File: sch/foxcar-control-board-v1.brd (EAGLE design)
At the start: 160 x 100 mm, 114 parts, among them J1 USB_MICROB, J2 MICROSD, J3 XBEE-PRO, U1 SPX29300, U2 HMC5883LSMD, U3 STM32F4V, U4 VNH5019, U6 MPU6000

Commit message: Making much better progress on stm32. relocating to house because I live in a land of less-than-24-hour coffee shops. :(
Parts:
- TP2: value TPTP06R -> (none)
- moved JP38 29.7 mm to (74.0, 33.3)
- moved JP37 28.2 mm to (76.8, 33.7)
- moved JP2 27.6 mm to (93.0, 33.3), turned to 180 degrees
- moved JP36 26.0 mm to (79.7, 33.3)
- moved JP35 23.5 mm to (82.5, 33.7)
- moved JP6 20.4 mm to (103.8, 33.3)
- moved C4 8.96 mm to (73.7, 42.2), turned to 270 degrees
- moved CTS1 6.33 mm to (77.8, 41.3)
- moved R14 5.72 mm to (35.2, 69.5)
- moved C5 4.24 mm to (81.9, 40.0), turned to 90 degrees
- moved C8 2.42 mm to (76.8, 45.4), turned to 0 degrees
- moved TP2 2.25 mm to (81.9, 45.1)
- moved C20 1.59 mm to (85.4, 43.2)
- moved R8 1.42 mm to (81.9, 43.2)
- moved C11 1.35 mm to (72.7, 65.4), turned to 270 degrees
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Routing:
- net N$16: track 0.00 -> 22.5 mm, vias 0 -> 1
- net N$10: track 0.00 -> 22.3 mm, vias 0 -> 1
- net N$9: track 0.00 -> 21.8 mm, vias 0 -> 1
- net N$14: track 0.00 -> 21.5 mm, vias 0 -> 1
- net TX2: track 0.00 -> 19.0 mm
- net RX1: track 0.00 -> 15.3 mm
- net TX1: track 0.00 -> 14.7 mm
- net OSC_IN1: track 0.00 -> 13.1 mm
- net OSC_OUT1: track 0.00 -> 12.5 mm
- net 3.3V: track 14.2 -> 25.8 mm
- net GND: track 7.37 -> 16.1 mm, vias 5 -> 13
- net NRST: track 0.00 -> 4.87 mm

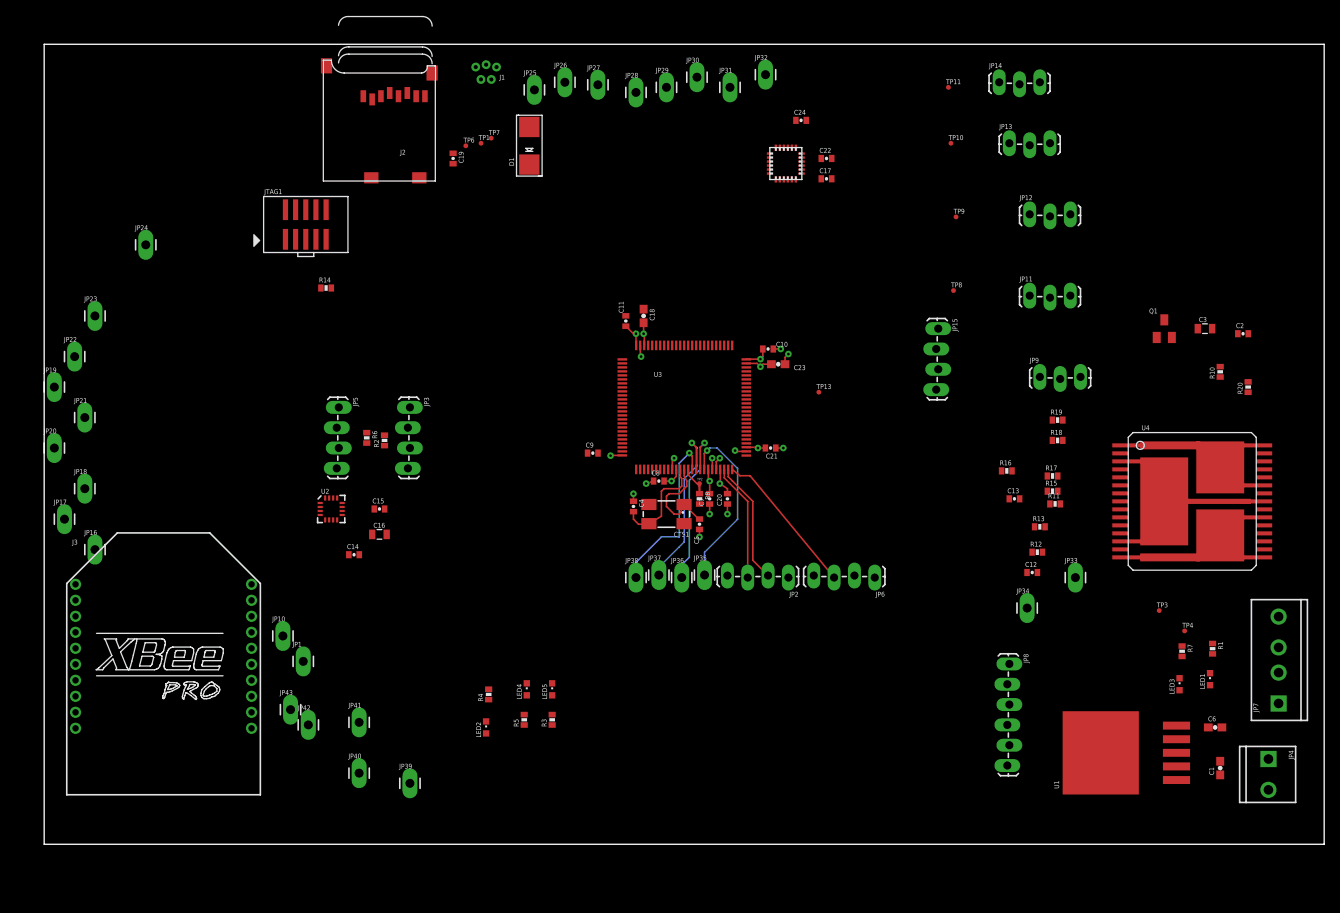
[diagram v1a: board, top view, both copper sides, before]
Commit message: Everything laid out except for the power stuff.
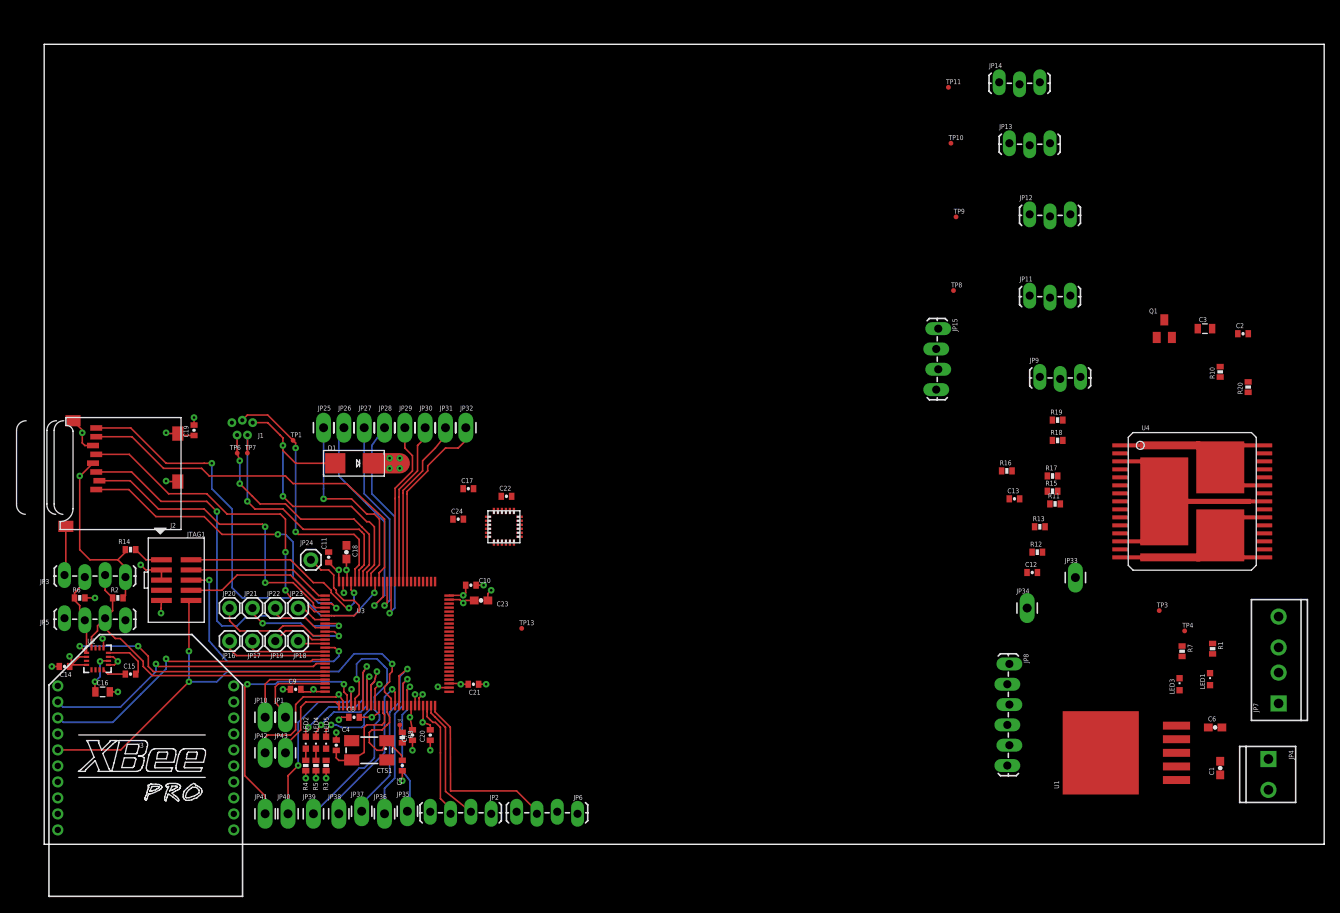
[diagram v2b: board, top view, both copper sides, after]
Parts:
- J1: value USB_MICROB -> (none)
- JP16, JP17, JP18, JP19, JP20, JP21, JP22, JP23, JP24: device SparkFun-Connectors:1X01_LONGPAD -> SparkFun-Connectors:1X01
- TP1, TP6, TP7: value TPTP06R -> (none)
- moved C24 65.7 mm to (51.8, 40.6)
- moved C17 59.2 mm to (53.0, 44.5)
- moved C22 58.2 mm to (57.8, 43.5)
- moved JP32 57.9 mm to (52.7, 52.1)
- moved U6 57.5 mm to (57.5, 39.7), turned to 90 degrees
- moved JP31 55.4 mm to (50.2, 52.1)
- moved JP30 55.4 mm to (47.6, 52.1)
- moved J1 53.9 mm to (24.8, 51.8)
- moved JP29 53.7 mm to (45.1, 52.1)
- moved JP28 52.4 mm to (42.5, 52.1)
- moved JP27 51.9 mm to (40.0, 52.1)
- moved JP26 51.3 mm to (37.5, 52.1)
- moved TP7 49.8 mm to (25.4, 48.9)
- moved JP25 49.8 mm to (34.9, 52.1)
- moved C8 48.2 mm to (38.7, 15.9)
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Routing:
- net NRST: track 4.87 -> 64.7 mm, vias 0 -> 3
- net SDIO_D1: track 0.00 -> 54.8 mm, vias 0 -> 2
- net SDIO_CMD: track 0.00 -> 49.2 mm, vias 0 -> 2
- net SDIO_D0: track 0.00 -> 48.3 mm
- net SCL1: track 0.00 -> 44.6 mm, vias 0 -> 2
- net SDIO_CLK: track 0.00 -> 42.3 mm, vias 0 -> 2
- net SDA1: track 0.00 -> 42.2 mm
- net SDIO_D2: track 0.00 -> 40.4 mm, vias 0 -> 2
- net FS_VBUS: track 0.00 -> 39.9 mm, vias 0 -> 2
- net SDIO_D3: track 0.00 -> 39.1 mm, vias 0 -> 2
- net 3.3V: track 25.8 -> 64.7 mm, vias 9 -> 17
- net TX_DIN1: track 0.00 -> 37.9 mm, vias 0 -> 1
- net RX_DOUT1: track 0.00 -> 36.8 mm, vias 0 -> 1
- net FS_DP: track 0.00 -> 33.3 mm, vias 0 -> 2
- net FS_DM: track 0.00 -> 33.0 mm, vias 0 -> 1
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
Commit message: Layout done, screenshots uploaded, parts list added.
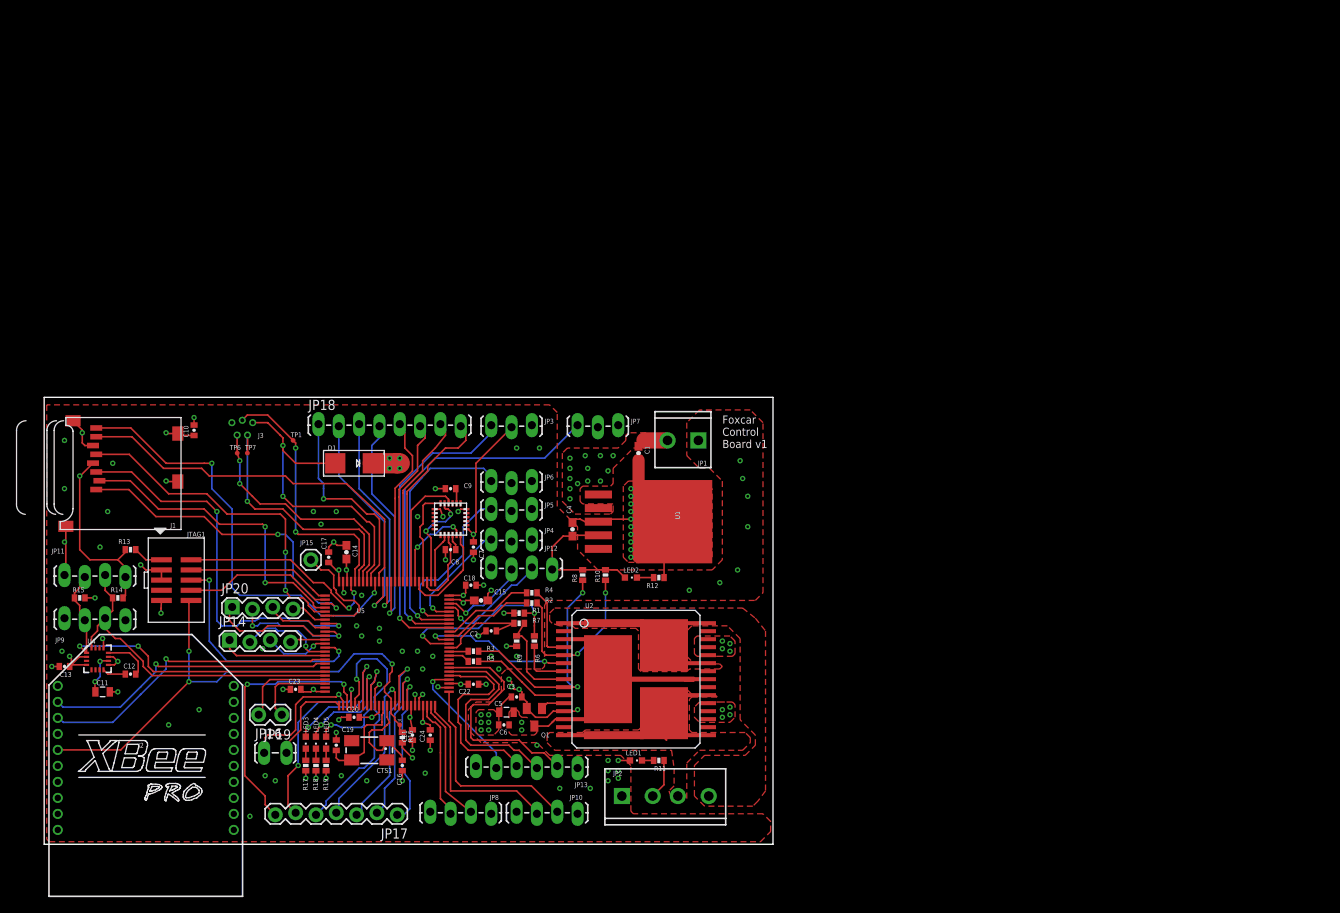
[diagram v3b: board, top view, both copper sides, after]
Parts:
- removed JP21, JP22, JP23, JP24: (no value), SparkFun-Connectors:1X01
- removed JP25, JP26, JP27, JP28, JP29, JP30, JP31, JP32, JP33, JP34, JP35, JP36, JP37, JP38, JP39, JP40, JP41, JP42, JP43: (no value), SparkFun-Connectors:1X01_LONGPAD
- removed R20: 4.7k, SparkFun-Passives:0402-RES
- removed TP10, TP11, TP13, TP3, TP4, TP8, TP9: TPTP06R, testpad:TP06R
- removed U6: MPU6000, invensense:QFN.24.4X4
- added R9: 1k, SparkFun-Passives:0402-RES
- added U5: STM32F4V, stm32f4:LQFP100
- C10: value 100nF -> 2.2uF
- C11: value 100nF -> 4.7uF; device SparkFun-Passives:0402-CAP -> SparkFun-Passives:0805
- C12: value 0.1uF -> 0.22uF
- C13: value 33nF -> 0.22uF
- C14, C15: value 0.22uF -> 2.2uF; device SparkFun-Passives:0402-CAP -> SparkFun-Passives:0603-CAP
- C16: value 4.7uF -> 16pF; device SparkFun-Passives:0805 -> SparkFun-Passives:0402-CAP
- C17, C22: value 0.1uF -> 100nF
- C18, C23: value 2.2uF -> 100nF; device SparkFun-Passives:0603-CAP -> SparkFun-Passives:0402-CAP
- C19: value 2.2uF -> 16pF
- C2: value 0.1uF -> 33nF
- C24: value 10nF -> 100nF
- C3: value 47uF -> 0.1uF; device SparkFun-Passives:0805 -> SparkFun-Passives:0402-CAP
- C4: value 16pF -> 10u; device SparkFun-Passives:0402-CAP -> SparkFun-Passives:0603-CAP
- C5: value 16pF -> 47uF; device SparkFun-Passives:0402-CAP -> SparkFun-Passives:0805
- C6: value 10u -> 0.1uF; device SparkFun-Passives:0603-CAP -> SparkFun-Passives:0402-CAP
- C7, C8: value 100nF -> 0.1uF
- C9: value 100nF -> 10nF
- J1: value (none) -> MICROSD; device SparkFun:MICRO-B-RA-TH -> adafruit:MICROSD
- J2: value MICROSD -> XBEE-PRO; device adafruit:MICROSD -> maxstream:XBEE-PRO
- J3: value XBEE-PRO -> (none); device maxstream:XBEE-PRO -> SparkFun:MICRO-B-RA-TH
- JP1: value (none) -> BATT; device SparkFun-Connectors:1X01_LONGPAD -> SparkFun-Connectors:SCREWTERMINAL-3.5MM-2_LOCK
- JP10: value (none) -> UART2; device SparkFun-Connectors:1X01_LONGPAD -> SparkFun-Connectors:1X04_LOCK_LONGPADS
- JP11: value ESCD -> I2C1-B; device SparkFun-Connectors:1X03_LOCK_LONGPADS -> SparkFun-Connectors:1X04_LOCK_LONGPADS
- JP12: value ESCC -> USART3; device SparkFun-Connectors:1X03_LOCK_LONGPADS -> SparkFun-Connectors:1X04_LOCK_LONGPADS
- JP13: value ESCB -> SPI1; device SparkFun-Connectors:1X03_LOCK_LONGPADS -> SparkFun-Connectors:1X06_LOCK_LONGPADS
- JP14: value ESCA -> (none); device SparkFun-Connectors:1X03_LOCK_LONGPADS -> SparkFun-Connectors:1X04_LOCK
- JP15: value USART3 -> (none); device SparkFun-Connectors:1X04_LOCK_LONGPADS -> SparkFun-Connectors:1X01
- JP16: device SparkFun-Connectors:1X01 -> SparkFun-Connectors:1X02_LOCK_LONGPADS
- JP17: device SparkFun-Connectors:1X01 -> SparkFun-Connectors:1X07_LOCK
- JP18: device SparkFun-Connectors:1X01 -> SparkFun-Connectors:1X08_LOCK_LONGPADS
- JP19: device SparkFun-Connectors:1X01 -> SparkFun-Connectors:1X02_LOCK
- JP2: value USART1 -> MOTORS; device SparkFun-Connectors:1X04_LOCK_LONGPADS -> SparkFun-Connectors:SCREWTERMINAL-3.5MM-4_LOCK
- JP20: device SparkFun-Connectors:1X01 -> SparkFun-Connectors:1X04_LOCK
- JP3: value I2C1-B -> SERVO; device SparkFun-Connectors:1X04_LOCK_LONGPADS -> SparkFun-Connectors:1X03_LOCK_LONGPADS
- JP4: value BATT -> ESCA; device SparkFun-Connectors:SCREWTERMINAL-3.5MM-2_LOCK -> SparkFun-Connectors:1X03_LOCK_LONGPADS
- JP5: value I2C1-A -> ESCB; device SparkFun-Connectors:1X04_LOCK_LONGPADS -> SparkFun-Connectors:1X03_LOCK_LONGPADS
- JP6: value UART2 -> ESCC; device SparkFun-Connectors:1X04_LOCK_LONGPADS -> SparkFun-Connectors:1X03_LOCK_LONGPADS
- JP7: value MOTORS -> ESCD; device SparkFun-Connectors:SCREWTERMINAL-3.5MM-4_LOCK -> SparkFun-Connectors:1X03_LOCK_LONGPADS
- JP8: value SPI1 -> USART1; device SparkFun-Connectors:1X06_LOCK_LONGPADS -> SparkFun-Connectors:1X04_LOCK_LONGPADS
- JP9: value SERVO -> I2C1-A; device SparkFun-Connectors:1X03_LOCK_LONGPADS -> SparkFun-Connectors:1X04_LOCK_LONGPADS
- LED2: value (none) -> GREEN
- LED3: value GREEN -> (none)
- R1: value 270 -> 10k
- R11: value 1k -> 270
- R12, R17, R18, R19: value 1k -> 50
- R13: value 1k -> 100
- R14: value 100 -> 1.5k
- R15: value 10k -> 1.5k
- R2, R6: value 1.5k -> 1k
- R3, R4, R5: value 50 -> 1k
- R7: value 50 -> 10k
- R8: value 10k -> 4.7k
- U2: value HMC5883LSMD -> VNH5019; device SparkFun-Sensors:16LPCC -> wicker:MULTIPOWERSO-30
- U3: value STM32F4V -> MPU6000; device stm32f4:LQFP100 -> invensense:QFN.24.4X4
- U4: value VNH5019 -> HMC5883LSMD; device wicker:MULTIPOWERSO-30 -> SparkFun-Sensors:16LPCC
- moved U4 138.3 mm to (6.67, 23.2), turned to 0 degrees
- moved JP11 125.6 mm to (2.54, 33.7)
- moved JP9 125.6 mm to (2.54, 28.3)
- moved R15 122.3 mm to (4.45, 30.8)
- moved C13 120.6 mm to (2.54, 22.2), turned to 180 degrees
- moved JP14 118.9 mm to (23.2, 25.4)
- moved R13 113.7 mm to (10.8, 36.8), turned to 180 degrees
- moved C12 113.4 mm to (10.8, 21.3)
- moved LED3 109.5 mm to (32.7, 12.7), turned to 180 degrees
- moved R18 101.2 mm to (34.0, 9.84), turned to 90 degrees
- moved R19 101.1 mm to (35.2, 9.84), turned to 90 degrees
- moved C2 101.1 mm to (55.9, 26.7), turned to 180 degrees
- moved JP4 101.0 mm to (55.9, 38.1), turned to 0 degrees
- moved R17 100.1 mm to (32.7, 9.84), turned to 90 degrees
- moved C3 97.6 mm to (59.1, 18.4), turned to 180 degrees
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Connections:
- removed net N$13: C17.1, U6.10
- removed net N$17: JP34.1, U3.PC4
- removed net N$8: JP33.1, U3.PC5
- new net REGOUT: C8.1, U3.10
- net 3.3V: now also C13.1, C14.2, C15.2, C17.2, C22.2, C24.2, C4.1, C7.1, J1.4, J2.1, J2.14, JP10.4, JP11.4, JP12.4, JP13.6, JP3.2, JP8.4, JP9.4, LED2.A, R13.2, R15.2, R16.2, R17.1, R18.1, R19.1, U3.13, U4.13, U4.2, U4.4, U5.VCAP1, U5.VCAP2, U5.VDD1, U5.VDD2, U5.VDD3, U5.VDD4, U5.VDD5, U5.VDD6, U5.VDDA; no longer C11.2, C14.1, C19.2, C22.1, C6.1, C7.2, C8.2, C9.2, J2.4, J3.1, J3.14, JP15.4, JP2.4, JP3.4, JP5.4, JP6.4, JP8.6, JP9.2, LED3.A, R2.2, R20.2, R3.1, R4.1, R5.1, R6.2, TP4.TP, U2.13, U2.2, U2.4, U3.VCAP1, U3.VCAP2, U3.VDD1, U3.VDD2, U3.VDD3, U3.VDD4, U3.VDD5, U3.VDD6, U3.VDDA, U6.13
- net CP: now also U2.11; no longer U4.11
- net CS: now also R7.2, R9.2, U2.8; no longer R11.2, R15.2, U4.8
- net DIR: now also JP3.1, U5.PE11; no longer JP9.1, TP13.TP, U3.PE11
- net ENA: now also R10.1, R2.2, U2.5; no longer R18.2, R20.1, U4.5
- net ENB: now also R3.2, R8.1, U2.9; no longer R10.1, R13.2, U4.9
- net ESCA: now also JP4.1, U5.PE15; no longer JP14.1, TP11.TP, U3.PE15
- net ESCB: now also JP5.1, U5.PE14; no longer JP13.1, TP10.TP, U3.PE14
- net ESCC: now also JP6.1, U5.PE13; no longer JP12.1, TP9.TP, U3.PE13
- net ESCD: now also JP7.1, U5.PE12; no longer JP11.1, TP8.TP, U3.PE12
- net FS_DM: now also J3.2, U5.PA11; no longer J1.2, U3.PA11
- net FS_DP: now also J3.3, U5.PA12; no longer J1.3, U3.PA12
- net FS_ID: now also J3.4, U5.PA10; no longer J1.4, U3.PA10
- net FS_VBUS: now also J3.1, U5.PA9; no longer J1.1, U3.PA9
- net GND: now also C11.2, C14.1, C15.1, C16.1, C17.1, C22.1, C24.1, C4.2, C5.2, C7.2, C8.2, C9.2, J1.6, J1.CD1, J1.CD2, J1.MT1, J1.MT2, J2.10, J3.5, JP1.1, JP10.1, JP11.1, JP12.1, JP13.1, JP2.2, JP3.3, JP9.1, R12.1, R9.1, U2.18, U2.19, U2.20, U2.26, U2.27, U2.28, U3.1, U3.18, U4.11, U4.9, U5.VREF+, U5.VSS1, U5.VSS2, U5.VSS3, U5.VSSA; no longer C11.1, C12.2, C14.2, C16.2, C17.2, C22.2, C24.2, C4.1, C5.1, C7.1, C8.1, C9.1, J1.5, J2.6, J2.CD1, J2.CD2, J2.MT1, J2.MT2, J3.10, JP15.1, JP2.1, JP3.1, JP4.1, JP5.1, JP6.1, JP7.2, JP9.3, R16.1, R7.1, U2.11, U2.9, U3.VREF+, U3.VSS1, U3.VSS2, U3.VSS3, U3.VSSA, U4.18, U4.19, U4.20, U4.26, U4.27, U4.28, U6.1, U6.18
- net IMU_CLKOUT: now also U3.22, U5.PD10; no longer U3.PD10, U6.22
- net IMU_FSYNC: now also U3.11, U5.PD9; no longer U3.PD9, U6.11
- net IMU_INT: now also U3.12, U5.PD8; no longer U3.PD8, U6.12
- net INA: now also R4.2, U2.4; no longer R19.2, U4.4
- net INB: now also R5.2, U2.10; no longer R12.2, U4.10
- net LED_B: now also U5.PC15; no longer U3.PC15
- net LED_G: now also U5.PC14; no longer U3.PC14
- net LED_R: now also LED3.A, U5.PC13; no longer LED2.A, U3.PC13
- net MD_CS: now also C2.1, R7.1, U5.PB2; no longer C13.1, R15.1, U3.PB2
- net MD_CSDIS: now also U2.6, U5.PE8; no longer U3.PE8, U4.6
- net MD_ENA: now also R2.1, U5.PE9; no longer R18.1, U3.PE9
- net MD_ENB: now also R3.1, U5.PB1; no longer R13.1, U3.PB1
- net MD_INA: now also R4.1, U5.PE10; no longer R19.1, U3.PE10
- net MD_INB: now also R5.1, U5.PB0; no longer R12.1, U3.PB0
- net MD_PWM: now also R1.2, R6.1, U5.PE7; no longer R16.2, R17.1, U3.PE7
- net N$1: now also JP18.1, U5.PA8; no longer JP25.1, U3.PA8
- net N$10: now also JP17.3, U5.PC1; no longer JP37.1, U3.PC1
- net N$11: now also C12.1, U4.8; no longer C15.1, U2.8
- net N$12: now also C11.1, U4.10; no longer C16.1, U2.10
- net N$14: now also JP17.2, U5.PC2; no longer JP36.1, U3.PC2
- net N$15: now also JP19.1, U5.PE1; no longer JP1.1, U3.PE1
- net N$16: now also JP17.1, U5.PC3; no longer JP35.1, U3.PC3
- net N$18: now also C9.1, U3.20; no longer C24.1, U6.20
- net N$2: now also LED2.C, R12.2; no longer LED3.C, R7.2
- net N$20: now also R13.1; no longer R14.1
- net N$3: now also R11.2; no longer R1.2
- net N$4: now also C12.2, U4.12; no longer C15.2, U2.12
- net N$41: now also JP16.2, U5.PE2; no longer JP43.1, U3.PE2
- net N$42: now also JP16.1, U5.PE3; no longer JP42.1, U3.PE3
- net N$43: now also JP17.7, U5.PE4; no longer JP41.1, U3.PE4
- net N$44: now also JP17.6, U5.PE5; no longer JP40.1, U3.PE5
- net N$45: now also JP17.5, U5.PE6; no longer JP39.1, U3.PE6
- net N$5: now also LED3.C, R17.2; no longer LED2.C, R4.2
- net N$55: now also JP18.2, U5.PC7; no longer JP26.1, U3.PC7
- net N$56: now also JP18.3, U5.PC6; no longer JP27.1, U3.PC6
- net N$57: now also JP18.4, U5.PD15; no longer JP28.1, U3.PD15
- net N$58: now also JP18.5, U5.PD14; no longer JP29.1, U3.PD14
- net N$59: now also JP18.6, U5.PD13; no longer JP30.1, U3.PD13
- net N$6: now also R18.2; no longer R5.2
- net N$60: now also JP18.7, U5.PD12; no longer JP31.1, U3.PD12
- net N$61: now also JP18.8, U5.PD11; no longer JP32.1, U3.PD11
- net N$66: now also JP19.2, U5.PE0; no longer JP10.1, U3.PE0
- net N$67: now also JP14.1, U5.PB5; no longer JP16.1, U3.PB5
- net N$68: now also JP14.2, U5.PB4; no longer JP17.1, U3.PB4
- net N$69: now also JP14.3, U5.PD7; no longer JP18.1, U3.PD7
- net N$7: now also R19.2; no longer R3.2
- net N$70: now also JP14.4, U5.PD6; no longer JP19.1, U3.PD6
- net N$71: now also U5.PD5; no longer U3.PD5
- net N$72: now also JP20.2, U5.PD4; no longer JP21.1, U3.PD4
- net N$73: now also JP20.3, U5.PD3; no longer JP22.1, U3.PD3
- net N$74: now also JP20.4, U5.PD1; no longer JP23.1, U3.PD1
- net N$75: now also JP15.1, U5.PD0; no longer JP24.1, U3.PD0
- net N$9: now also JP17.4, U5.PC0; no longer JP38.1, U3.PC0
- net NRST: now also J2.5, R16.1, U5.NRST; no longer J3.5, R8.1, U3.NRST
- net OSC_IN1: now also C19.2, U5.PH0; no longer C4.2, U3.PH0
- net OSC_OUT1: now also C16.2, U5.PH1; no longer C5.2, U3.PH1
- net OUTA: now also JP2.4, U2.1, U2.25, U2.30, U2.OUTA, U2.OUTA@1; no longer JP7.4, U4.1, U4.25, U4.30, U4.OUTA, U4.OUTA@1
- net OUTB: now also JP2.3, U2.15, U2.16, U2.21, U2.OUTB, U2.OUTB@1; no longer JP7.3, U4.15, U4.16, U4.21, U4.OUTB, U4.OUTB@1
- net PWM: now also R6.2, U2.7; no longer R17.2, U4.7
- net RX1: now also JP8.2, U5.PA1; no longer JP2.2, U3.PA1
- net RX2: now also JP10.2, U5.PA3; no longer JP6.2, U3.PA3
- net RX3: now also JP12.2, U5.PB11; no longer JP15.2, U3.PB11
- net RX_DOUT1: now also J2.2, U5.PB7; no longer J3.2, U3.PB7
- net SCL1: now also JP11.2, JP9.2, R15.1, U4.1, U5.PB8; no longer JP3.2, JP5.2, R6.1, U2.1, U3.PB8
- net SDA1: now also JP11.3, JP9.3, R14.1, U4.16, U5.PB9; no longer JP3.3, JP5.3, R2.1, U2.16, U3.PB9
- net SDIO_CLK: now also J1.5, U5.PC12; no longer J2.5, U3.PC12
- net SDIO_CMD: now also J1.3, U5.PD2; no longer J2.3, U3.PD2
- net SDIO_D0: now also J1.7, U5.PC8; no longer J2.7, U3.PC8
- net SDIO_D1: now also J1.8, U5.PC9; no longer J2.8, U3.PC9
- net SDIO_D2: now also J1.1, U5.PC10; no longer J2.1, U3.PC10
- net SDIO_D3: now also J1.2, U5.PC11; no longer J2.2, U3.PC11
- net SPI1_MISO: now also JP13.3, U5.PA6; no longer JP8.3, U3.PA6
- net SPI1_MOSI: now also JP13.2, U5.PA7; no longer JP8.2, U3.PA7
- net SPI1_NSS: now also JP13.5, U5.PA4; no longer JP8.5, U3.PA4
- net SPI1_SCK: now also JP13.4, U5.PA5; no longer JP8.4, U3.PA5
- net SPI2_CS: now also U3.8, U5.PB12; no longer U3.PB12, U6.8
- net SPI2_MISO: now also U3.9, U5.PB14; no longer U3.PB14, U6.9
- net SPI2_MOSI: now also U3.24, U5.PB15; no longer U3.PB15, U6.24
- net SPI2_SCK: now also U3.23, U5.PB13; no longer U3.PB13, U6.23
- net TCK: now also U5.PA14; no longer U3.PA14
- net TDI: now also U5.PA15; no longer U3.PA15
- net TDO: now also U5.PB3; no longer U3.PB3
- net TMS: now also U5.PA13; no longer U3.PA13
- net TX1: now also JP8.3, U5.PA0; no longer JP2.3, U3.PA0
- net TX2: now also JP10.3, U5.PA2; no longer JP6.3, U3.PA2
- net TX3: now also JP12.3, U5.PB10; no longer JP15.3, U3.PB10
- net TX_DIN1: now also J2.3, U5.PB6; no longer J3.3, U3.PB6
- net VCC: now also C5.1, C6.1, U2.13, U2.23, U2.3, U2.VCC, U2.VCC@1; no longer C2.1, C3.1, U4.13, U4.23, U4.3, U4.VCC, U4.VCC@1
- net VIN: now also C3.1, JP1.2, JP2.1, U2.12; no longer C12.1, JP4.2, JP7.1, TP3.TP, U4.12
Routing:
- net GND: track 45.5 -> 100.2 mm, vias 22 -> 99
- net ESCD: track 0.00 -> 46.5 mm, vias 0 -> 1
- net 3.3V: track 64.7 -> 103.3 mm, vias 17 -> 19
- net DIR: track 0.00 -> 38.3 mm, vias 0 -> 1
- net ESCC: track 0.00 -> 32.6 mm, vias 0 -> 1
- net SPI1_MOSI: track 0.00 -> 29.7 mm
- net ENB: track 0.00 -> 29.3 mm, vias 0 -> 2
- net SPI1_MISO: track 0.00 -> 27.2 mm
- net RX2: track 0.00 -> 25.8 mm
- net SPI1_SCK: track 0.00 -> 25.6 mm
- net MD_PWM: track 0.00 -> 24.2 mm, vias 0 -> 2
- net ESCB: track 0.00 -> 21.8 mm, vias 0 -> 1
- net ENA: track 0.00 -> 21.6 mm, vias 0 -> 2
- net MD_CSDIS: track 0.00 -> 19.3 mm, vias 0 -> 2
- net VIN: track 3.37 -> 21.7 mm, vias 4 -> 27
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- added copper zone on layer 1, net GND
- added copper zone on layer 1, net OUTA
- added copper zone on layer 1, net OUTB
- added copper zone on layer 1, net VCC
- added copper zone on layer 1, net VIN
- added copper zone on layer 2, net VIN
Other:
- board size 160 x 100 mm -> 91.1 x 55.9 mm
- board text added: "Foxcar Control Board v1"
